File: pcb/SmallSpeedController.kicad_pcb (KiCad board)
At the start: 4 copper layers, 30.7 x 51.7 mm, 37 parts, among them J1 Conn_01x02_Socket, J10 Conn_01x03_Socket, J11 Conn_01x03_Socket, J2 Conn_01x02_Socket, J4 Conn_01x02_Socket, J5 Conn_01x04_Socket, J6 Conn_01x04_Socket, J9 Conn_01x03_Socket, SW2 TS-1088-AR02016, U1 AP62300TWU, U2 AMS1117-3.3, U3 DRV8837DSGR, U4 DRV8837DSGR, U5 CH32V003FxUx

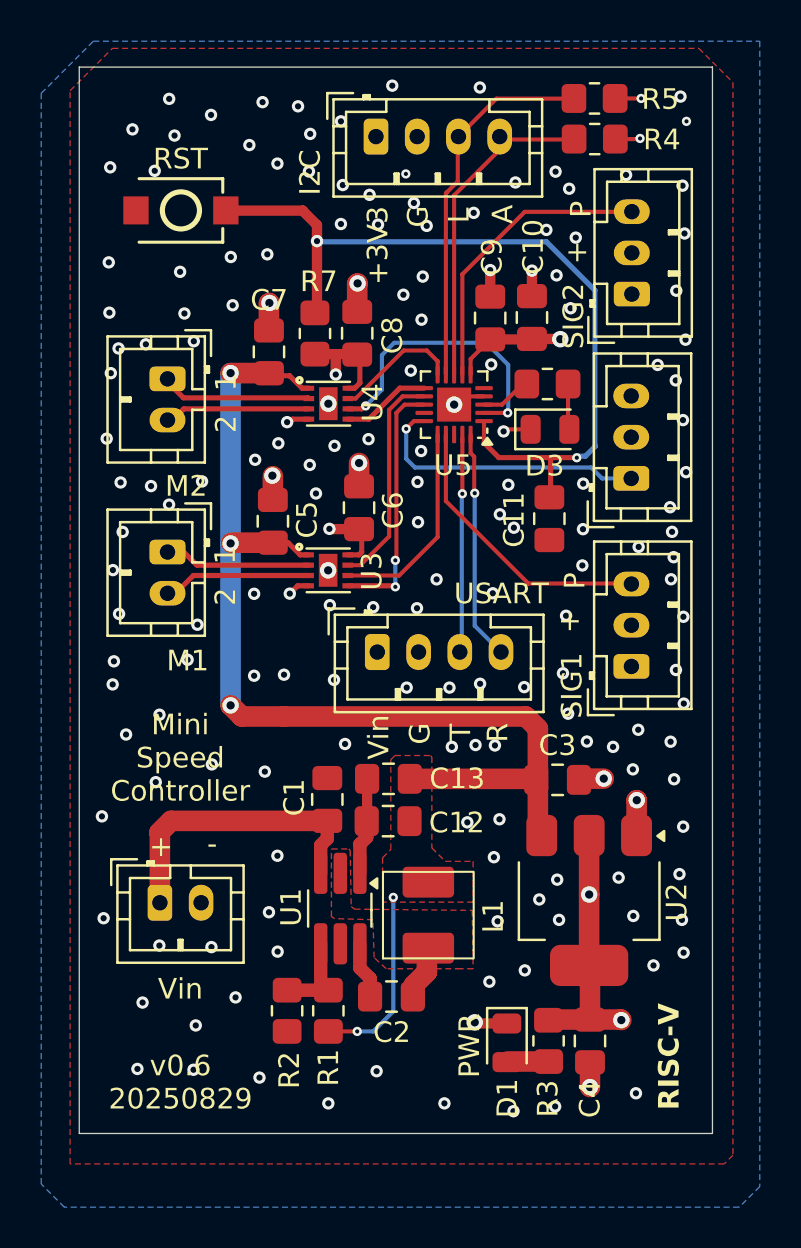
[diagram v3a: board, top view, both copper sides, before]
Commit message: pcb: harmonize silk prints, also use double vias for 7V rails
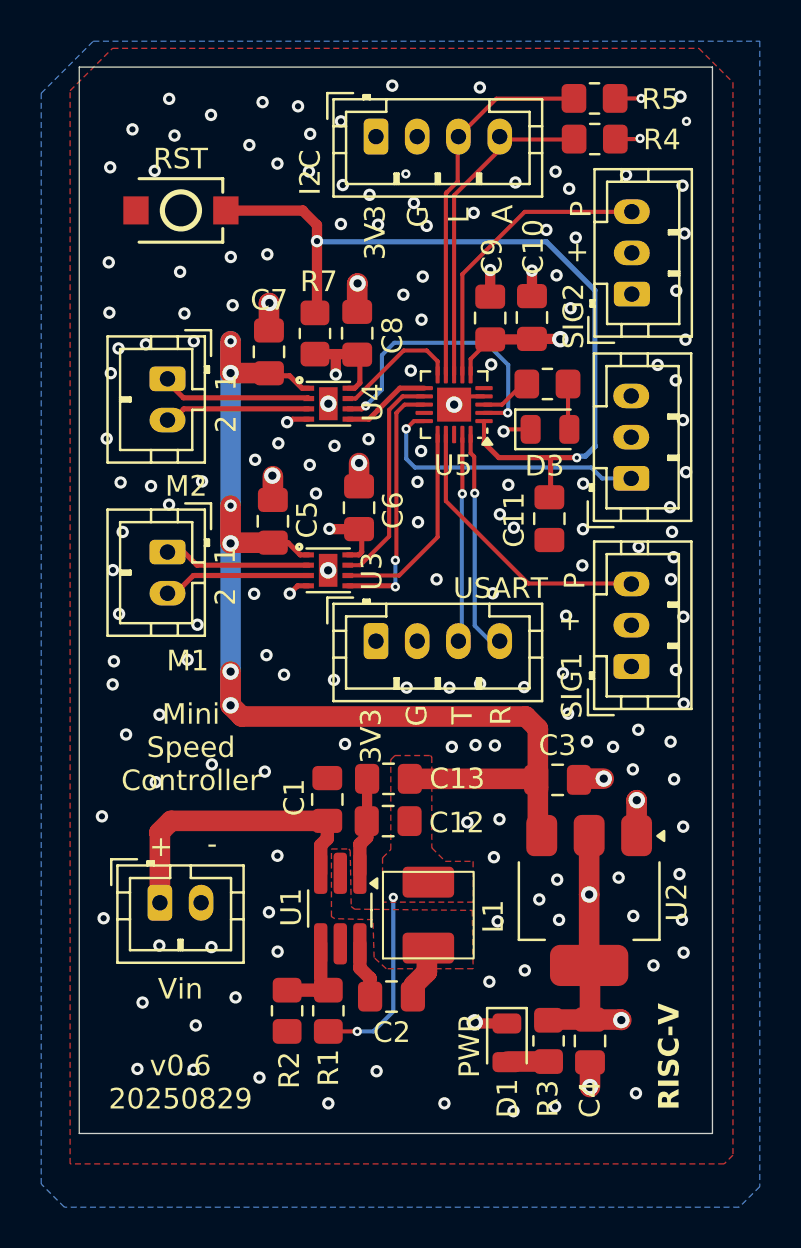
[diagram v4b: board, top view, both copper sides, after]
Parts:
- moved J6 0.53 mm to (33.9, 96.1)
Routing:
- net /V_dcdc: track 60.0 -> 66.5 mm, vias 5 -> 8
- net GND: vias 174 -> 171
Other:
- board text added: "3V3"
- board text removed: "+3V3"
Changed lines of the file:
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@@
 	(footprint "Connector_JST:JST_PH_B4B-PH-K_1x04_P2.00mm_Vertical"
 		(layer "F.Cu")
-		(at 33.975 96.65)
+		(at 33.91 96.12)
 		(descr "JST PH series connector, B4B-PH-K (http://www.jst-mfg.com/product/pdf/eng/ePH.pdf), generated with kicad-footprint-generator")
 		(tags "connector JST PH vertical")
@@
 	)
 	(gr_text "USART"
-		(at 39.99 93.82 0)
+		(at 39.95 93.56 0)
 		(layer "F.SilkS")
 		(effects
@@
 	)
 	(gr_text "G"
-		(at 36.63 101.14 90)
+		(at 36.48 100.26 90)
 		(layer "F.SilkS")
 		(effects
@@
 		)
 	)
-	(gr_text "+3V3"
-		(at 34 76.93 90)
+	(gr_text "3V3"
+		(at 33.87 76.3 90)
 		(layer "F.SilkS")
 		(effects
@@
 	)
 	(gr_text "R"
-		(at 40.4 101.04 90)
+		(at 40.55 100.21 90)
 		(layer "F.SilkS")
 		(effects
@@
 	)
 	(gr_text "Mini\nSpeed\nController"
-		(at 24.42 103.98 0)
+		(at 24.94 103.47 0)
 		(layer "F.SilkS")
 		(effects
@@
 	)
 	(gr_text "T"
-		(at 38.6 100.96 90)
+		(at 38.68 100.16 90)
 		(layer "F.SilkS")
 		(effects
@@
 		)
 	)
-	(gr_text "Vin"
-		(at 34.63 101.87 90)
+	(gr_text "3V3"
+		(at 34.256248 102.065 90)
 		(layer "F.SilkS")
 		(effects
@@
 	)
 	(via
-		(at 28 97.8)
+		(at 28.6 96.8)
 		(size 0.6)
 		(drill 0.3)
@@
 	)
 	(via
-		(at 33.775 94.475)
-		(size 0.6)
-		(drill 0.3)
-		(layers "F.Cu" "B.Cu")
-		(free yes)
-		(net 2)
-	)
-	(via
 		(at 39.81 109.71)
 		(size 0.6)
@@
 	)
 	(via
-		(at 35.9 94.525)
-		(size 0.6)
-		(drill 0.3)
-		(layers "F.Cu" "B.Cu")
-		(free yes)
-		(net 2)
-	)
-	(via
 		(at 43.96 88.48)
 		(size 0.6)
@@
 	)
 	(via
-		(at 31.675 94.375)
-		(size 0.6)
-		(drill 0.3)
-		(layers "F.Cu" "B.Cu")
-		(free yes)
-		(net 2)
-	)
-	(via
 		(at 25.06 116.91)
 		(size 0.6)
@@
 	)
 	(segment
+		(start 26.86 99.235)
+		(end 26.86 97.6)
+		(width 1)
+		(layer "F.Cu")
+		(net 27)
+	)
+	(segment
 		(start 30.65125 83.855)
 		(end 30.325 83.855)
@@
 	)
 	(segment
+		(start 26.86 83.12)
+		(end 26.86 81.58)
+		(width 1)
+		(layer "F.Cu")
+		(net 27)
+	)
+	(segment
 		(start 30.2375 91.9375)
 		(end 29.65 91.35)
@@
 	)
 	(segment
-		(start 29.45 99.775)
-		(end 27.4 99.775)
+		(start 27.4 99.775)
+		(end 41.175 99.775)
 		(width 1)
 		(layer "F.Cu")
@@
 	)
 	(segment
-		(start 29.45 99.775)
-		(end 41.175 99.775)
-		(width 1)
-		(layer "F.Cu")
-		(net 27)
-	)
-	(segment
 		(start 41.3725 102.8)
 		(end 41.7625 103.19)
@@
 		(net 27)
 	)
+	(segment
+		(start 26.86 91.38)
+		(end 26.86 89.55)
+		(width 1)
+		(layer "F.Cu")
+		(net 27)
+	)
+	(via
+		(at 26.86 89.55)
+		(size 0.6)
+		(drill 0.3)
+		(layers "F.Cu" "B.Cu")
+		(net 27)
+	)
 	(via
 		(at 26.86 99.235)
@@
 	)
 	(via
+		(at 26.86 97.6)
+		(size 0.8)
+		(drill 0.4)
+		(layers "F.Cu" "B.Cu")
+		(net 27)
+	)
+	(via
 		(at 33 115.05)
 		(size 0.45)
@@
 	)
 	(via
+		(at 26.86 81.58)
+		(size 0.6)
+		(drill 0.3)
+		(layers "F.Cu" "B.Cu")
+		(net 27)
+	)
+	(via
 		(at 26.86 91.38)
 		(size 0.8)
@@
 	)
 	(segment
+		(start 26.86 83.12)
+		(end 26.86 81.58)
+		(width 1)
+		(layer "B.Cu")
+		(net 27)
+	)
+	(segment
 		(start 34.75 114.08)
 		(end 33.78 115.05)
@@
 	)
 	(segment
-		(start 26.86 83.12)
+		(start 26.86 89.55)
 		(end 26.86 91.38)
 		(width 1)
@@
 	)
 	(segment
-		(start 26.86 99.235)
+		(start 26.86 97.6)
 		(end 26.86 91.38)
 		(width 1)
@@
 	)
 	(segment
+		(start 26.86 83.12)
+		(end 26.86 89.55)
+		(width 1)
+		(layer "B.Cu")
+		(net 27)
+	)
+	(segment
 		(start 33.78 115.05)
 		(end 33 115.05)
@@
 		(layer "B.Cu")
 		(net 27)
+	)
+	(segment
+		(start 26.86 99.235)
+		(end 26.86 97.6)
+		(width 1)
+		(layer "B.Cu")
+		(net 27)

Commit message: pcb: non functional changes
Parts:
- moved J6 0.71 mm to (34.1, 96.8)
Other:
- board text removed: "3V3"
- board text removed: "G"
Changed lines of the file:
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@@
 	(footprint "Connector_JST:JST_PH_B4B-PH-K_1x04_P2.00mm_Vertical"
 		(layer "F.Cu")
-		(at 33.91 96.12)
+		(at 34.07 96.81)
 		(descr "JST PH series connector, B4B-PH-K (http://www.jst-mfg.com/product/pdf/eng/ePH.pdf), generated with kicad-footprint-generator")
 		(tags "connector JST PH vertical")
@@
 		(layer "Edge.Cuts")
 	)
-	(gr_text "G"
-		(at 35.95 75.53 90)
+	(gr_text "-"
+		(at 36 75.47 90)
 		(layer "F.SilkS")
 		(effects
@@
 	)
 	(gr_text "USART"
-		(at 39.95 93.56 0)
+		(at 40.47 94.04 0)
 		(layer "F.SilkS")
 		(effects
@@
 		)
 	)
-	(gr_text "G"
-		(at 36.48 100.26 90)
+	(gr_text "-"
+		(at 36.49 101.48 90)
 		(layer "F.SilkS")
 		(effects
@@
 		)
 	)
-	(gr_text "3V3"
-		(at 33.87 76.3 90)
+	(gr_text "+"
+		(at 33.78 75.45 90)
 		(layer "F.SilkS")
 		(effects
@@
 	)
 	(gr_text "R"
-		(at 40.55 100.21 90)
+		(at 40.78 101.35 90)
 		(layer "F.SilkS")
 		(effects
@@
 	)
 	(gr_text "Mini\nSpeed\nController"
-		(at 24.94 103.47 0)
+		(at 24.93 104.03 0)
 		(layer "F.SilkS")
 		(effects
@@
 	)
 	(gr_text "T"
-		(at 38.68 100.16 90)
+		(at 38.71 101.22 90)
 		(layer "F.SilkS")
 		(effects
@@
 		)
 	)
-	(gr_text "3V3"
-		(at 34.256248 102.065 90)
+	(gr_text "+"
+		(at 34.46 101.48 90)
 		(layer "F.SilkS")
 		(effects
